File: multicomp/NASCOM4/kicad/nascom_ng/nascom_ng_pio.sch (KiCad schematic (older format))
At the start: 6 parts, among them U1 Z80PIO, U13 Z80CTC

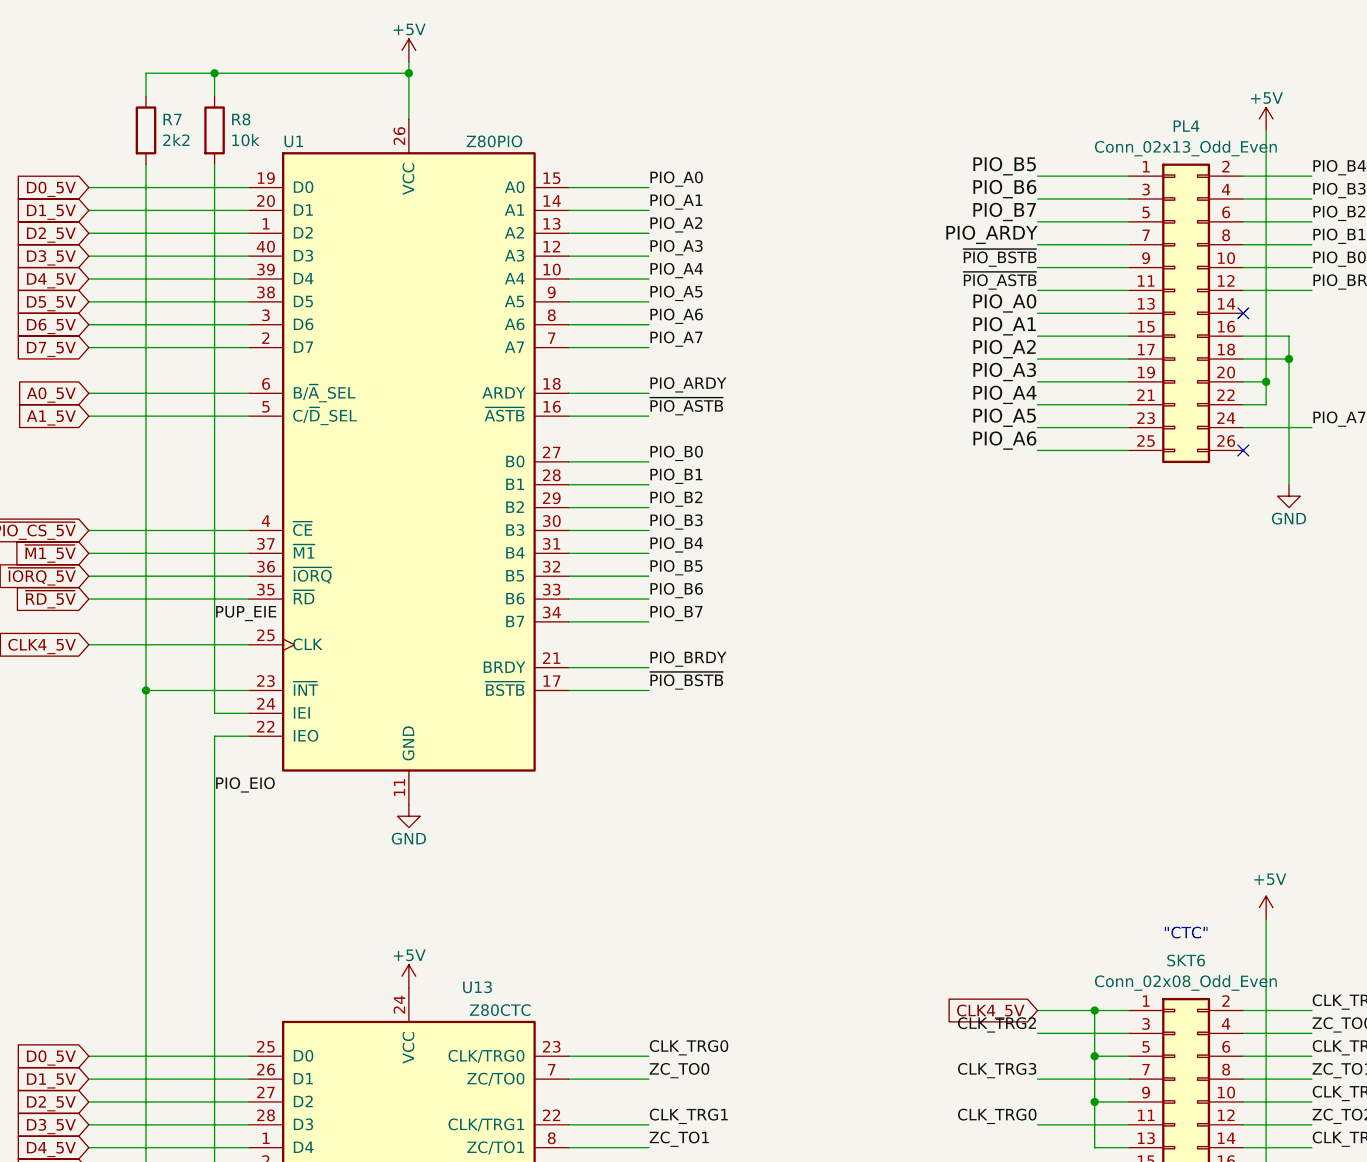
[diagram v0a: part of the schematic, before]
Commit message: All nets routed, ref designators resequenced, nearly finished!
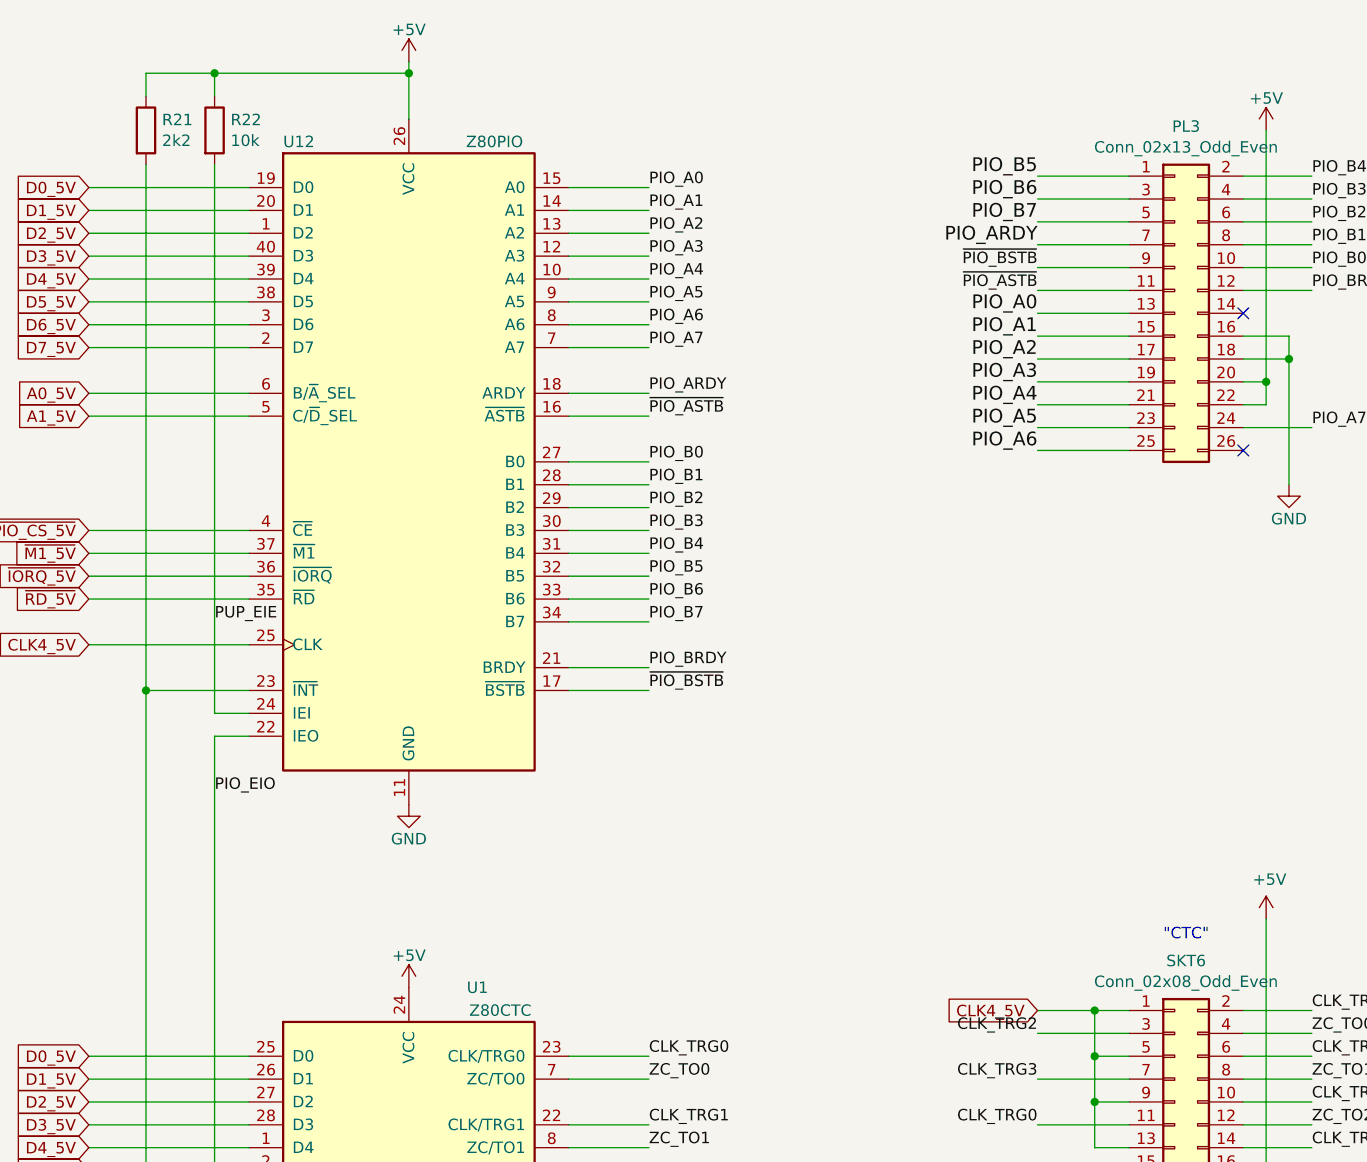
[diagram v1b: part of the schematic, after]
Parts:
- renumbered PL4 to PL3, R7 to R21, R8 to R22, U13 to U1, U1 to U12
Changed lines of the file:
@@
 $EndDescr
 $Comp
-L myLib:Z80PIO U1
+L myLib:Z80PIO U12
 U 1 1 5FC9E4CC
 P 4400 2500
-F 0 "U1" H 3850 3900 50  0000 L CNN
+F 0 "U12" H 3850 3900 50  0000 L CNN
 F 1 "Z80PIO" H 4650 3900 50  0000 L CNN
 F 2 "Package_DIP:DIP-40_W15.24mm" H 4400 2900 50  0001 C CNN
@@
 ~M1_5V
 $Comp
-L Device:R R8
+L Device:R R22
 U 1 1 5FD27F88
 P 3550 1050
-F 0 "R8" H 3620 1096 50  0000 L CNN
+F 0 "R22" H 3620 1096 50  0000 L CNN
 F 1 "10k" H 3620 1005 50  0000 L CNN
 F 2 "Resistor_THT:R_Axial_DIN0204_L3.6mm_D1.6mm_P7.62mm_Horizontal" V 3480 1050 50  0001 C CNN
@@
 PIO is first device on interrupt\ndaisy-chain
 $Comp
-L Device:R R7
+L Device:R R21
 U 1 1 5FD2D67B
 P 3250 1050
-F 0 "R7" H 3320 1096 50  0000 L CNN
+F 0 "R21" H 3320 1096 50  0000 L CNN
 F 1 "2k2" H 3320 1005 50  0000 L CNN
 F 2 "Resistor_THT:R_Axial_DIN0204_L3.6mm_D1.6mm_P7.62mm_Horizontal" V 3180 1050 50  0001 C CNN
@@
 ~PIO_BSTB
 $Comp
-L Connector_Generic:Conn_02x13_Odd_Even PL4
+L Connector_Generic:Conn_02x13_Odd_Even PL3
 U 1 1 60828C59
 P 7750 1850
-F 0 "PL4" H 7800 2667 50  0000 C CNN
+F 0 "PL3" H 7800 2667 50  0000 C CNN
 F 1 "Conn_02x13_Odd_Even" H 7800 2576 50  0000 C CNN
 F 2 "Connector_IDC:IDC-Header_2x13_P2.54mm_Vertical" H 7750 1850 50  0001 C CNN
@@
 CLK_TRG2
 $Comp
-L myLib:Z80CTC U13
+L myLib:Z80CTC U1
 U 1 1 60F2EDA1
 P 4400 6100
-F 0 "U13" H 4700 7400 50  0000 C CNN
+F 0 "U1" H 4700 7400 50  0000 C CNN
 F 1 "Z80CTC" H 4800 7300 50  0000 C CNN
 F 2 "Package_DIP:DIP-28_W15.24mm" H 4400 6350 50  0001 C CNN

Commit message: Files for REV A release to PCB manufacture
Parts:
- renumbered SKT6 to J4, PL3 to PL4
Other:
- note added: ""PORTS""
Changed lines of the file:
@@
 ~PIO_BSTB
 $Comp
-L Connector_Generic:Conn_02x13_Odd_Even PL3
+L Connector_Generic:Conn_02x13_Odd_Even PL4
 U 1 1 60828C59
 P 7750 1850
-F 0 "PL3" H 7800 2667 50  0000 C CNN
+F 0 "PL4" H 7800 2667 50  0000 C CNN
 F 1 "Conn_02x13_Odd_Even" H 7800 2576 50  0000 C CNN
 F 2 "Connector_IDC:IDC-Header_2x13_P2.54mm_Vertical" H 7750 1850 50  0001 C CNN
 F 3 "~" H 7750 1850 50  0001 C CNN
 	1    7750 1850
-	1    0    0    -1
-$EndComp
-$Comp
-L Connector_Generic:Conn_02x08_Odd_Even PL?
-U 1 1 60EDA1EF
-P 7750 5200
-AR Path="/5FC877BB/60EDA1EF" Ref="PL?"  Part="1"
-AR Path="/5FC85C78/60EDA1EF" Ref="PL?"  Part="1"
-AR Path="/5FC8753B/60EDA1EF" Ref="SKT6"  Part="1"
-F 0 "SKT6" H 7800 5717 50  0000 C CNN
-F 1 "Conn_02x08_Odd_Even" H 7800 5626 50  0000 C CNN
-F 2 "Connector_IDC:IDC-Header_2x08_P2.54mm_Vertical" H 7750 5200 50  0001 C CNN
-F 3 "~" H 7750 5200 50  0001 C CNN
-	1    7750 5200
 	1    0    0    -1
 $EndComp
@@
 Text Notes 7050 6800 0    98   ~ 20
 Z80-PIO, Z80-CTC and their connectors
+Text Notes 7650 950  0    50   ~ 0
+"PORTS"
+$Comp
+L Connector_Generic:Conn_02x08_Odd_Even PL?
+U 1 1 60EDA1EF
+P 7750 5200
+AR Path="/5FC877BB/60EDA1EF" Ref="PL?"  Part="1"
+AR Path="/5FC85C78/60EDA1EF" Ref="PL?"  Part="1"
+AR Path="/5FC8753B/60EDA1EF" Ref="J4"  Part="1"
+F 0 "J4" H 7800 5717 50  0000 C CNN
+F 1 "Conn_02x08_Odd_Even" H 7800 5626 50  0000 C CNN
+F 2 "Connector_IDC:IDC-Header_2x08_P2.54mm_Vertical" H 7750 5200 50  0001 C CNN
+F 3 "~" H 7750 5200 50  0001 C CNN
+	1    7750 5200
+	1    0    0    -1
+$EndComp
 $EndSCHEMATC
